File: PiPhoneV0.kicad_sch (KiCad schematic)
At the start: 48 parts, among them J1 GPIO, J2 Conn_01x40_MountingPin, J3 Conn_01x15_MountingPin, SW1 SW_Push, SW10 SW_Push, SW11 SW_Push, SW12 SW_Push, SW13 SW_Push, SW14 SW_Push, SW15 SW_Push, SW16 SW_Push, SW17 SW_Push, SW18 SW_Push, SW2 SW_Push, SW3 SW_Push, SW4 SW_Push, SW5 SW_Push, SW6 SW_Push, SW7 SW_Push, SW8 SW_Push, SW9 SW_Push, U1 ICN6211, U2 TPS61165DRV

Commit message: chore: chill out drc a bit more
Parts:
- SW1, SW10, SW11, SW12, SW13, SW14, SW15, SW16, SW17, SW18, SW2, SW3, SW4, SW5, SW6, SW7, SW8, SW9: footprint 1 key-switches.pretty:SW_MX_LowProfile_THT -> 1 key-switches.pretty:SW_Gateron_LowProfile_THT
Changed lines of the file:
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@@
 			)
 		)
-		(property "Footprint" "1 key-switches.pretty:SW_MX_LowProfile_THT"
+		(property "Footprint" "1 key-switches.pretty:SW_Gateron_LowProfile_THT"
 			(at 157.48 82.55 0)
 			(effects
@@
 			)
 		)
-		(property "Footprint" "1 key-switches.pretty:SW_MX_LowProfile_THT"
+		(property "Footprint" "1 key-switches.pretty:SW_Gateron_LowProfile_THT"
 			(at 177.8 59.69 0)
 			(effects
@@
 			)
 		)
-		(property "Footprint" "1 key-switches.pretty:SW_MX_LowProfile_THT"
+		(property "Footprint" "1 key-switches.pretty:SW_Gateron_LowProfile_THT"
 			(at 198.12 93.98 0)
 			(effects
@@
 			)
 		)
-		(property "Footprint" "1 key-switches.pretty:SW_MX_LowProfile_THT"
+		(property "Footprint" "1 key-switches.pretty:SW_Gateron_LowProfile_THT"
 			(at 177.8 93.98 0)
 			(effects
@@
 			)
 		)
-		(property "Footprint" "1 key-switches.pretty:SW_MX_LowProfile_THT"
+		(property "Footprint" "1 key-switches.pretty:SW_Gateron_LowProfile_THT"
 			(at 198.12 71.12 0)
 			(effects
@@
 			)
 		)
-		(property "Footprint" "1 key-switches.pretty:SW_MX_LowProfile_THT"
+		(property "Footprint" "1 key-switches.pretty:SW_Gateron_LowProfile_THT"
 			(at 177.8 71.12 0)
 			(effects
@@
 			)
 		)
-		(property "Footprint" "1 key-switches.pretty:SW_MX_LowProfile_THT"
+		(property "Footprint" "1 key-switches.pretty:SW_Gateron_LowProfile_THT"
 			(at 157.48 36.83 0)
 			(effects
@@
 			)
 		)
-		(property "Footprint" "1 key-switches.pretty:SW_MX_LowProfile_THT"
+		(property "Footprint" "1 key-switches.pretty:SW_Gateron_LowProfile_THT"
 			(at 177.8 48.26 0)
 			(effects
@@
 			)
 		)
-		(property "Footprint" "1 key-switches.pretty:SW_MX_LowProfile_THT"
+		(property "Footprint" "1 key-switches.pretty:SW_Gateron_LowProfile_THT"
 			(at 198.12 59.69 0)
 			(effects
@@
 			)
 		)
-		(property "Footprint" "1 key-switches.pretty:SW_MX_LowProfile_THT"
+		(property "Footprint" "1 key-switches.pretty:SW_Gateron_LowProfile_THT"
 			(at 177.8 82.55 0)
 			(effects
@@
 			)
 		)
-		(property "Footprint" "1 key-switches.pretty:SW_MX_LowProfile_THT"
+		(property "Footprint" "1 key-switches.pretty:SW_Gateron_LowProfile_THT"
 			(at 177.8 36.83 0)
 			(effects
@@
 			)
 		)
-		(property "Footprint" "1 key-switches.pretty:SW_MX_LowProfile_THT"
+		(property "Footprint" "1 key-switches.pretty:SW_Gateron_LowProfile_THT"
 			(at 198.12 82.55 0)
 			(effects
@@
 			)
 		)
-		(property "Footprint" "1 key-switches.pretty:SW_MX_LowProfile_THT"
+		(property "Footprint" "1 key-switches.pretty:SW_Gateron_LowProfile_THT"
 			(at 157.48 71.12 0)
 			(effects
@@
 			)
 		)
-		(property "Footprint" "1 key-switches.pretty:SW_MX_LowProfile_THT"
+		(property "Footprint" "1 key-switches.pretty:SW_Gateron_LowProfile_THT"
 			(at 157.48 93.98 0)
 			(effects
@@
 			)
 		)
-		(property "Footprint" "1 key-switches.pretty:SW_MX_LowProfile_THT"
+		(property "Footprint" "1 key-switches.pretty:SW_Gateron_LowProfile_THT"
 			(at 157.48 48.26 0)
 			(effects
@@
 			)
 		)
-		(property "Footprint" "1 key-switches.pretty:SW_MX_LowProfile_THT"
+		(property "Footprint" "1 key-switches.pretty:SW_Gateron_LowProfile_THT"
 			(at 157.48 59.69 0)
 			(effects
@@
 			)
 		)
-		(property "Footprint" "1 key-switches.pretty:SW_MX_LowProfile_THT"
+		(property "Footprint" "1 key-switches.pretty:SW_Gateron_LowProfile_THT"
 			(at 198.12 36.83 0)
 			(effects
@@
 			)
 		)
-		(property "Footprint" "1 key-switches.pretty:SW_MX_LowProfile_THT"
+		(property "Footprint" "1 key-switches.pretty:SW_Gateron_LowProfile_THT"
 			(at 198.12 48.26 0)
 			(effects

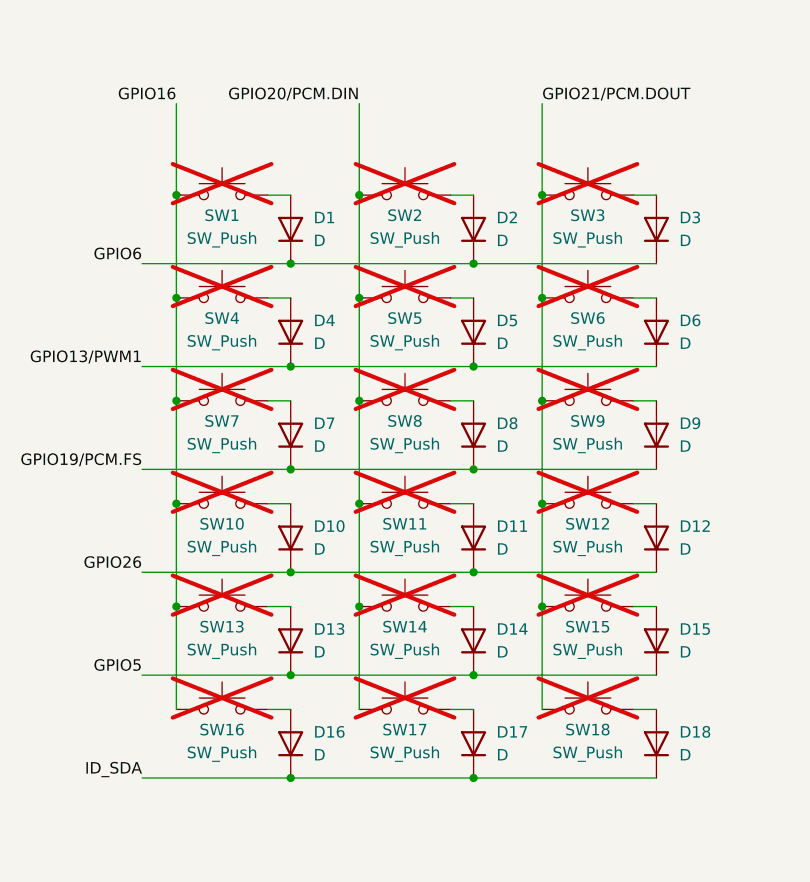
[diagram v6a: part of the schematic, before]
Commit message: feat: 3d models for everything!
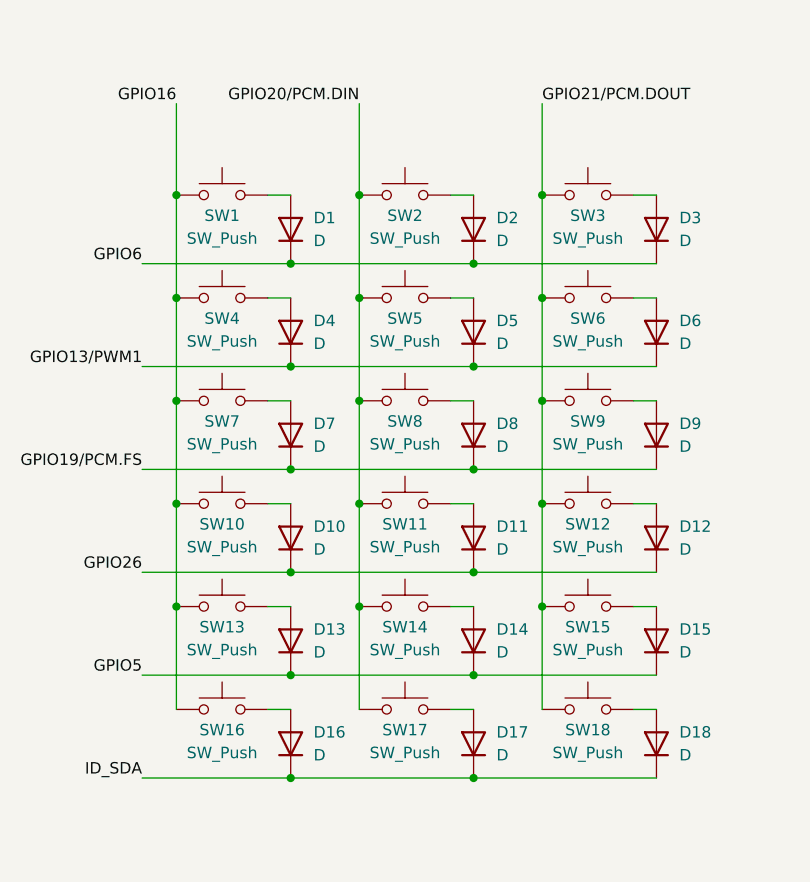
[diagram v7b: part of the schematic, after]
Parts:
- L1: footprint Inductor_SMD:L_6.3x6.3_H3 -> EasyEDA:IND-SMD_L5.0-W5.0-P3.60_SMNR5040
- SW1, SW10, SW11, SW12, SW13, SW14, SW15, SW16, SW17, SW18, SW2, SW3, SW4, SW5, SW6, SW7, SW8, SW9: now fitted
- U1: footprint Package_DFN_QFN:QFN-48-1EP_6x6mm_P0.4mm_EP4.2x4.2mm -> EasyEDA:QFN-48_L6.0-W6.0-P0.40-TL-EP4.2
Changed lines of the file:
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@@
 		(in_bom yes)
 		(on_board yes)
-		(dnp yes)
+		(dnp no)
 		(property "Reference" "SW13"
 			(at 157.48 89.916 0)
@@
 		(in_bom yes)
 		(on_board yes)
-		(dnp yes)
+		(dnp no)
 		(property "Reference" "SW8"
 			(at 177.8 67.056 0)
@@
 		(in_bom yes)
 		(on_board yes)
-		(dnp yes)
+		(dnp no)
 		(property "Reference" "SW18"
 			(at 198.12 101.346 0)
@@
 		(in_bom yes)
 		(on_board yes)
-		(dnp yes)
+		(dnp no)
 		(property "Reference" "SW17"
 			(at 177.8 101.346 0)
@@
 			)
 		)
-		(property "Footprint" "Package_DFN_QFN:QFN-48-1EP_6x6mm_P0.4mm_EP4.2x4.2mm"
+		(property "Footprint" "EasyEDA:QFN-48_L6.0-W6.0-P0.40-TL-EP4.2"
 			(at 455.93 67.31 0)
 			(effects
@@
 		(in_bom yes)
 		(on_board yes)
-		(dnp yes)
+		(dnp no)
 		(property "Reference" "SW12"
 			(at 198.12 78.486 0)
@@
 		(in_bom yes)
 		(on_board yes)
-		(dnp yes)
+		(dnp no)
 		(property "Reference" "SW11"
 			(at 177.8 78.486 0)
@@
 		(in_bom yes)
 		(on_board yes)
-		(dnp yes)
+		(dnp no)
 		(property "Reference" "SW1"
 			(at 157.48 44.196 0)
@@
 		(in_bom yes)
 		(on_board yes)
-		(dnp yes)
+		(dnp no)
 		(property "Reference" "SW5"
 			(at 177.8 55.626 0)
@@
 		(in_bom yes)
 		(on_board yes)
-		(dnp yes)
+		(dnp no)
 		(property "Reference" "SW9"
 			(at 198.12 67.056 0)
@@
 		(in_bom yes)
 		(on_board yes)
-		(dnp yes)
+		(dnp no)
 		(property "Reference" "SW14"
 			(at 177.8 89.916 0)
@@
 		(in_bom yes)
 		(on_board yes)
-		(dnp yes)
+		(dnp no)
 		(property "Reference" "SW2"
 			(at 177.8 44.196 0)
@@
 		(in_bom yes)
 		(on_board yes)
-		(dnp yes)
+		(dnp no)
 		(property "Reference" "SW15"
 			(at 198.12 89.916 0)
@@
 		(in_bom yes)
 		(on_board yes)
-		(dnp yes)
+		(dnp no)
 		(property "Reference" "SW10"
 			(at 157.48 78.486 0)
@@
 		(in_bom yes)
 		(on_board yes)
-		(dnp yes)
+		(dnp no)
 		(property "Reference" "SW16"
 			(at 157.48 101.346 0)
@@
 			)
 		)
-		(property "Footprint" "Inductor_SMD:L_6.3x6.3_H3"
+		(property "Footprint" "EasyEDA:IND-SMD_L5.0-W5.0-P3.60_SMNR5040"
 			(at 488.95 138.43 0)
 			(effects
@@
 		(in_bom yes)
 		(on_board yes)
-		(dnp yes)
+		(dnp no)
 		(property "Reference" "SW4"
 			(at 157.48 55.626 0)
@@
 		(in_bom yes)
 		(on_board yes)
-		(dnp yes)
+		(dnp no)
 		(property "Reference" "SW7"
 			(at 157.48 67.056 0)
@@
 		(in_bom yes)
 		(on_board yes)
-		(dnp yes)
+		(dnp no)
 		(property "Reference" "SW3"
 			(at 198.12 44.196 0)
@@
 		(in_bom yes)
 		(on_board yes)
-		(dnp yes)
+		(dnp no)
 		(property "Reference" "SW6"
 			(at 198.12 55.626 0)
